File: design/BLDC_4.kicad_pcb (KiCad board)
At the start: 4 copper layers, 55 x 77 mm, 152 parts, among them J1 Conn_01x03, J2 Conn_01x02, J3 Conn_02x06_Odd_Even, J4 Conn_01x01_Pin, J5 Conn_01x01_Pin, J6 Conn_02x06_Odd_Even, K1 SERVO, P101 CANBUS, P2 SWD, P3 PWR_COMM, Q1 IRFS7530, Q2 IRFS7530, Q3 IRFS7530, Q4 IRFS7530, Q5 IRFS7530, Q6 IRFS7530, U1 STM32F40X_LQFP64, U2 TC2117, U3 DRV8302, U4 INA826AIDR, U401 SN65HVD232, U5 AM26LV32xD, U6 OPA333AIDBVR, U7 INA826AIDR, U8 MAX485ED, U9 OPA333AIDBVR, X1 MINI-USB-SHIELD-32005-201, X2 8MHz 10ppm

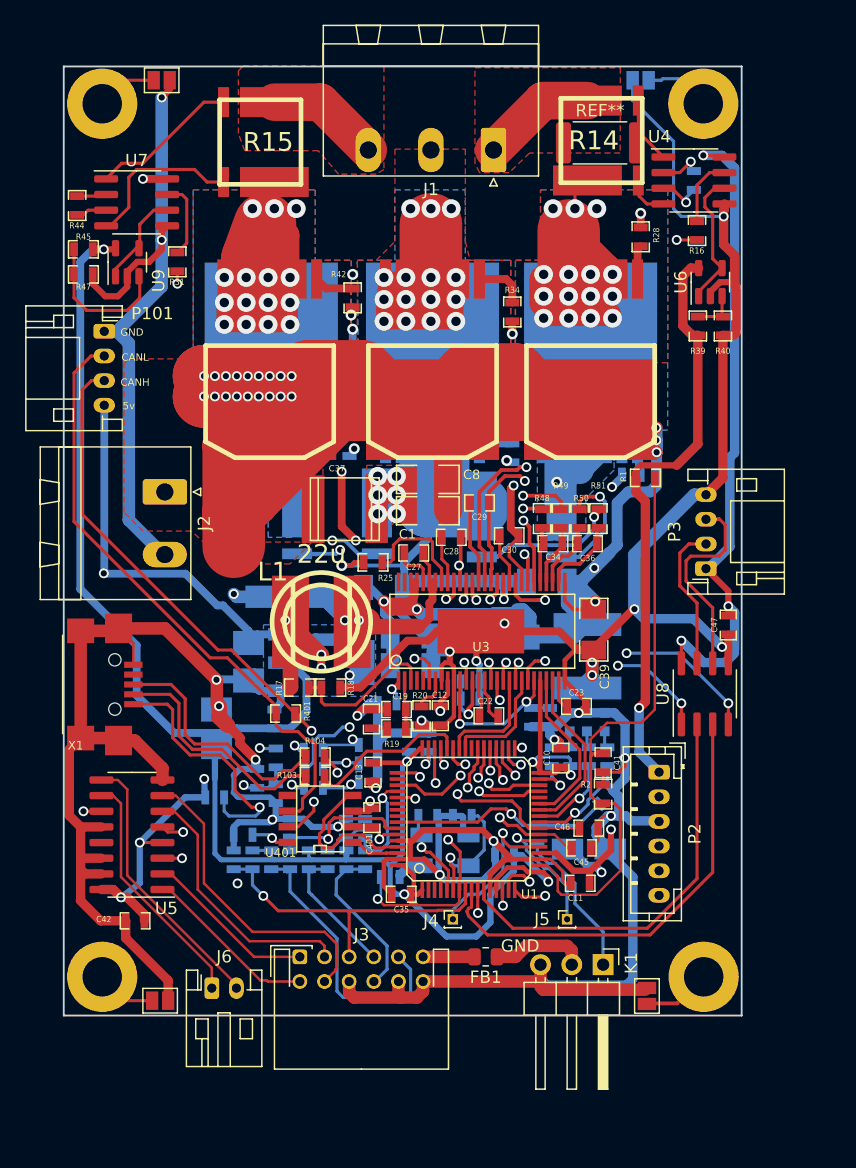
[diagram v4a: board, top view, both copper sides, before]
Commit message: Limpando warnings e DRC errors
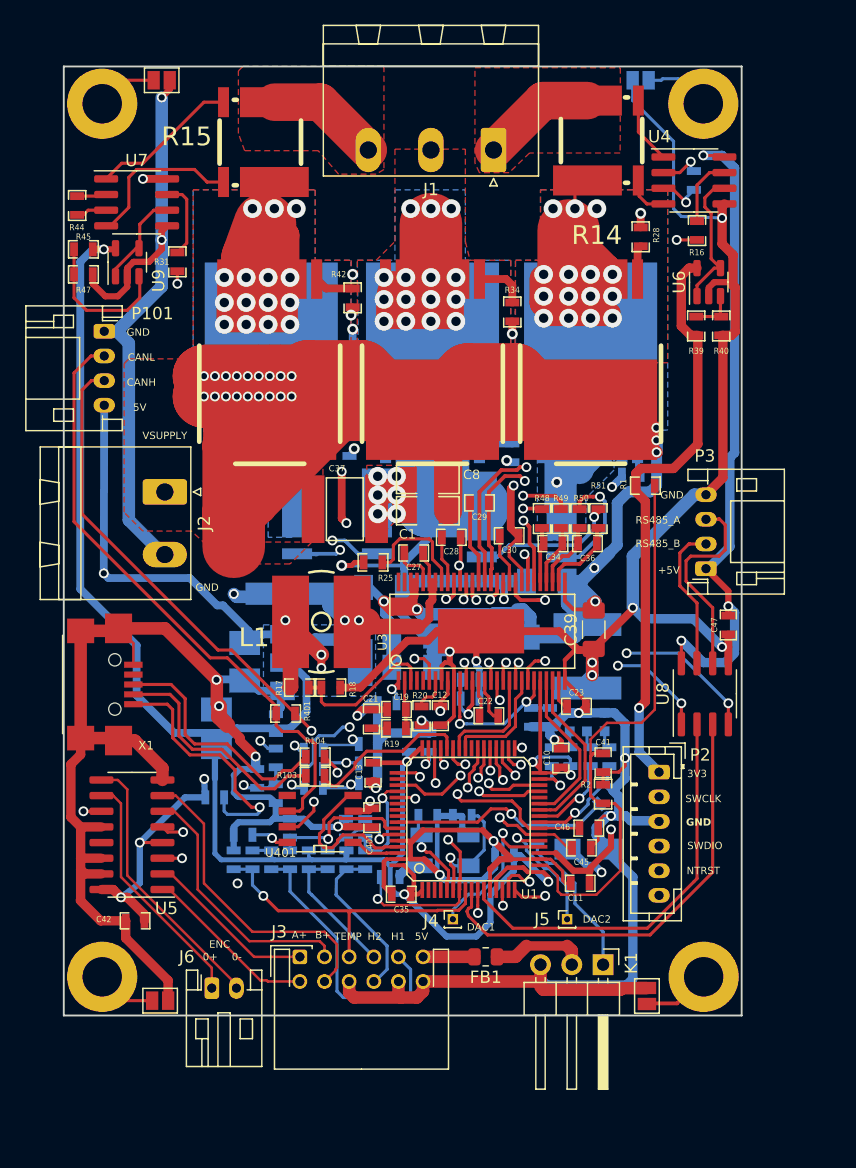
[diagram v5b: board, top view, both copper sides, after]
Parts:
- removed REF**: R_2512_6332Metric, Resistor_SMD:R_2512_6332Metric
- C25, C33: footprint w_smd_cap:c_tant_B -> CRF1:c_tant_B
- C39: footprint CRF1:SMD-1206 -> Capacitor_SMD:C_1206_3216Metric_Pad1.33x1.80mm_HandSolder
- C51: footprint w_smd_cap:c_2220 -> CRF1:c_2220
- D5: footprint w_smd_diode:do214ac -> CRF1:do214ac
- U2: footprint CRF1:SOT-223 -> Package_TO_SOT_SMD:SOT-223
- moved R1 0.64 mm to (115.2, 104.0)
- moved C24 0.40 mm to (85.2, 123.3)
- moved C33 0.32 mm to (82.7, 118.3)
- moved D4 0.25 mm to (87.0, 112.8)
- moved C49 0.18 mm to (96.3, 118.7)
- moved R37 0.17 mm to (112.3, 126.0)
- moved R38 0.14 mm to (110.7, 126.0)
- moved R39 0.13 mm to (119.3, 91.1)
- moved U6 0.13 mm to (120.3, 87.5)
- moved R40 0.13 mm to (121.3, 91.1)
- moved C26 0.13 mm to (101.0, 119.8)
- moved C44 0.13 mm to (96.3, 116.2)
- moved R24 0.09 mm to (92.7, 128.1)
- moved R33 0.08 mm to (92.7, 125.0)
- turned U2 to 0 degrees
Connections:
- C3 pad 2: GND -> /MCU/SERVO
- R39 pad 2: GND -> Net-(U6-+)
- R40 pad 1: GND -> Net-(U6-+)
- R5 pad 1: GND -> /MCU/SERVO
- U1 pad 57: GND -> /MCU/SERVO
- U6 pad 3: GND -> Net-(U6-+)
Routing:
- net GND: track 596.3 -> 566.8 mm, vias 34 -> 31
- net /MCU/SERVO: track 0.00 -> 18.1 mm, vias 0 -> 1
- net Net-(U6-+): track 0.00 -> 3.72 mm
- net VCC: track 268.6 -> 266.3 mm, vias 11 -> 10
- net /MCU/ADC_TEMP: track 48.9 -> 47.3 mm
- net V_SUPPLY: track 315.9 -> 314.8 mm
- net +5V: track 261.3 -> 260.2 mm
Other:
- board text added: "+5V"
- board text added: "0+"
- board text added: "0-"
- board text added: "3V3"
- board text added: "5V"
- board text added: "A+"
- board text added: "A-"
- board text added: "B+"
- board text added: "B-"
- board text added: "DAC1"
- board text added: "DAC2"
- board text added: "ENC"
- board text added: "NTRST"
- board text added: "RS485_A"
- board text added: "RS485_B"
- board text added: "SERVO"
- board text added: "SWCLK"
- board text added: "SWDIO"
- board text added: "VSUPPLY"
- board text removed: "3.3V"
- board text removed: "3.3v"
- board text removed: "5v"
- board text removed: "ADC"
- board text removed: "ADC2"
- board text removed: "CLK"
- board text removed: "DIO"
- board text removed: "MISO"
- board text removed: "MOSI"
- board text removed: "RST"
- board text removed: "RX"
- board text removed: "SCL"
- board text removed: "SDA"
- board text removed: "TX"

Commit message: Final 20230228
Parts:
- removed R54: SHUNT, CRF1:WSLP2726
- added JP10: SolderJumper_2_Bridged, JRM_Footprint:MicroNetSep, F.Cu at (81.9, 77.1)
- added JP11: SolderJumper_2_Bridged, JRM_Footprint:MicroNetSep, F.Cu at (112.8, 79.5)
- added JP12: SolderJumper_2_Bridged, JRM_Footprint:MicroNetSep, F.Cu at (112.8, 80.6)
- added JP5: SolderJumper_2_Bridged, JRM_Footprint:MicroNetSep, B.Cu at (104.5, 108.6)
- added JP6: SolderJumper_2_Bridged, JRM_Footprint:MicroNetSep, B.Cu at (105.4, 108.6)
- added JP7: SolderJumper_2_Bridged, JRM_Footprint:MicroNetSep, B.Cu at (89.6, 108.6)
- added JP8: SolderJumper_2_Bridged, JRM_Footprint:MicroNetSep, B.Cu at (92.3, 108.6)
- added JP9: SolderJumper_2_Bridged, JRM_Footprint:MicroNetSep, F.Cu at (81.9, 78.1)
- added R52: YLR12-3-8F-W, JRM_Footprint:YLR2512_G4, B.Cu at (104.8, 105.7)
- R14, R15, R53: value SHUNT -> YLR12-3-8F-W; footprint CRF1:WSLP2726 -> JRM_Footprint:YLR2512_G4
- U2: footprint Package_TO_SOT_SMD:SOT-223 -> CRF1:SOT-223
- moved R53 14.9 mm to (90.5, 105.7), turned to 90 degrees
- moved R14 5.62 mm to (109.3, 79.8), turned to 0 degrees
- moved R15 4.18 mm to (84.8, 79.2), turned to 0 degrees
- moved U2 0.13 mm to (88.8, 118.4), turned to 90 degrees
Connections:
- R14 pad 1: /Power MOSFETS/PHASE_1 -> /Mosfet driver/H1_VS
- R14 pad 2: /Mosfet driver/H1_VS -> /Power MOSFETS/PHASE_1
- R53 pad 1: GND -> /Mosfet driver/H3_LOW
- R53 pad 2: /Mosfet driver/H1_LOW -> GND
- U4 pad 1: Net-(U4--) -> Net-(JP11-A)
- U4 pad 4: Net-(U4-+) -> Net-(JP12-A)
- U7 pad 1: Net-(U7--) -> Net-(JP10-A)
- U7 pad 4: Net-(U7-+) -> Net-(JP9-A)
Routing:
- net Net-(JP9-A): track 0.00 -> 13.6 mm
- net Net-(U7-+): track 13.3 -> 0.00 mm
- net Net-(U7--): track 12.1 -> 0.00 mm
- net Net-(JP10-A): track 0.00 -> 10.6 mm
- net GND: track 566.8 -> 575.1 mm
- net /Mosfet driver/H1_LOW: track 48.5 -> 54.1 mm
- net Net-(U4--): track 5.41 -> 0.00 mm
- net /Power MOSFETS/PHASE_1: track 9.28 -> 14.2 mm
- net /Mosfet driver/SH1_A: track 23.9 -> 19.4 mm
- net /Mosfet driver/H3_LOW: track 57.0 -> 61.4 mm
- net /Power MOSFETS/PHASE_3: track 9.23 -> 13.3 mm
- net Net-(JP11-A): track 0.00 -> 4.06 mm
- net Net-(JP12-A): track 0.00 -> 3.96 mm
- net Net-(U4-+): track 3.53 -> 0.00 mm
- net /Mosfet driver/H3_VS: track 160.6 -> 163.6 mm
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- added copper zone on B.Cu, net GND

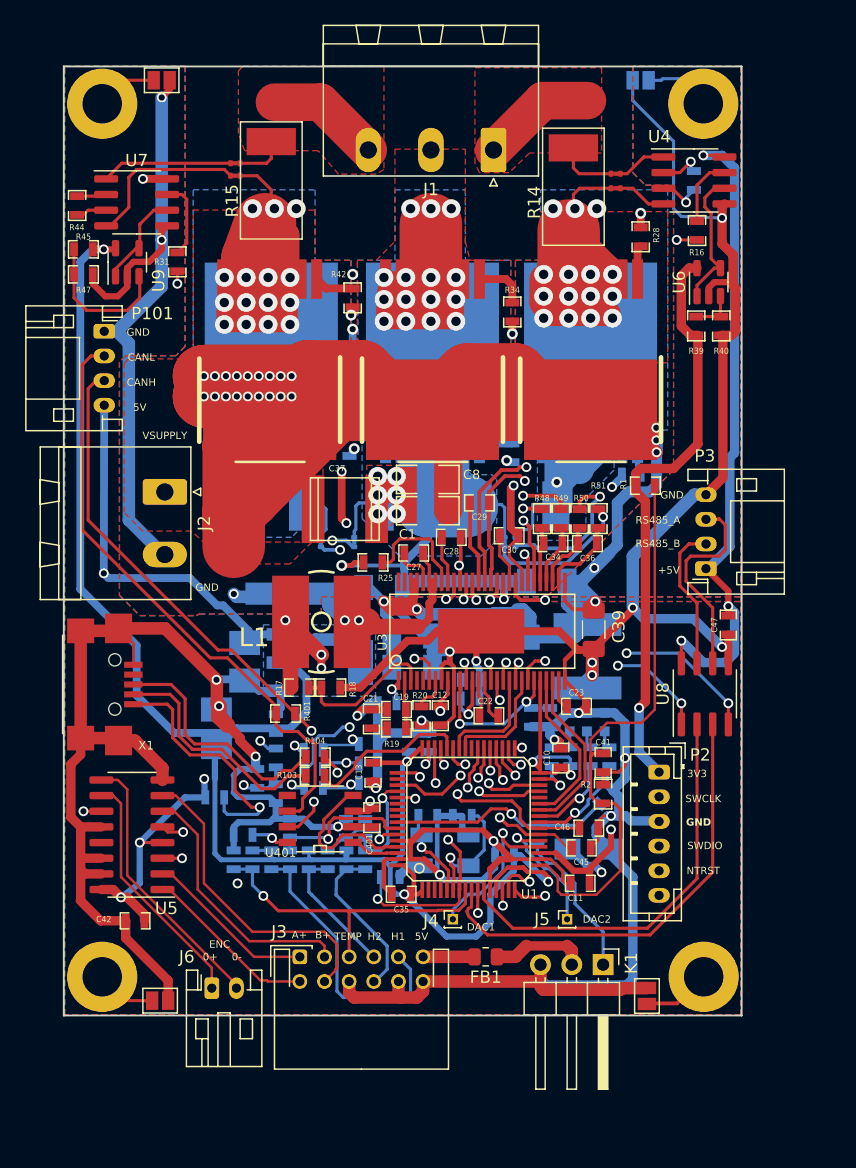
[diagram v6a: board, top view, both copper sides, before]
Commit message: Fixing voltage supply of INA826 to read phase current value
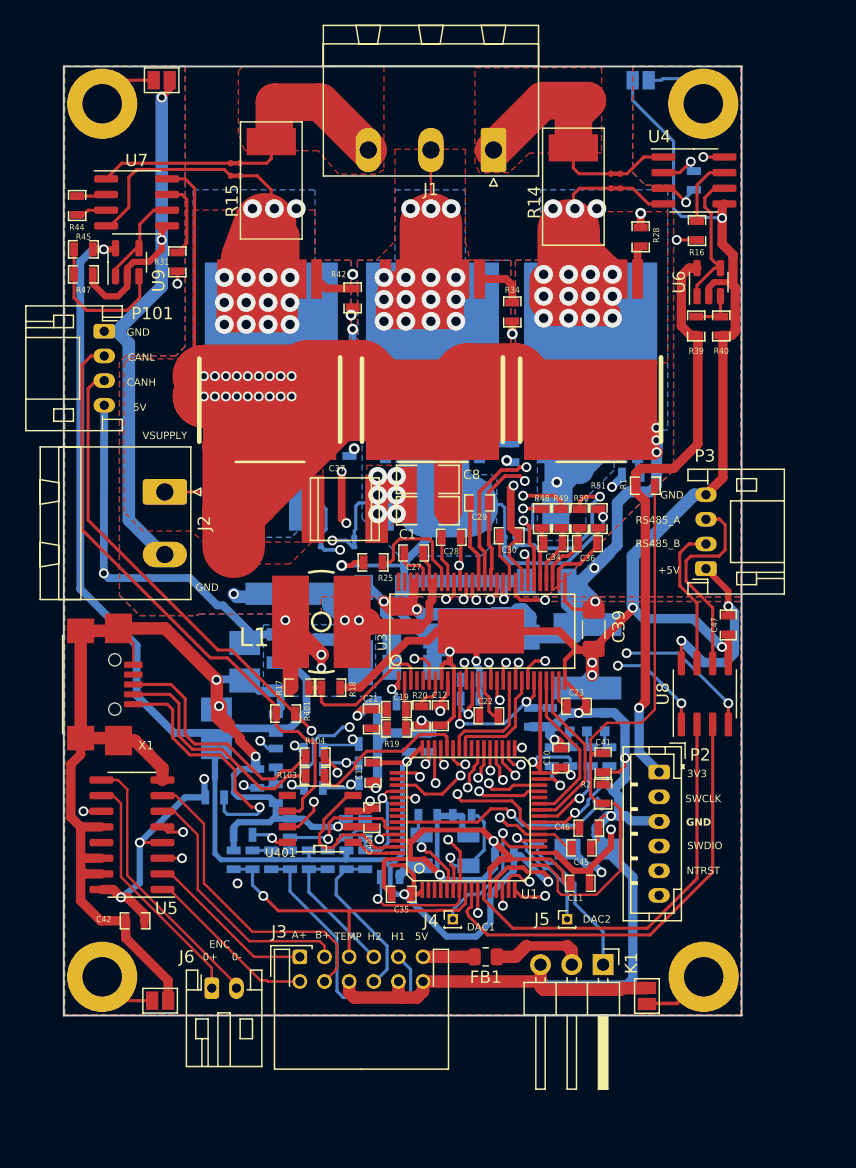
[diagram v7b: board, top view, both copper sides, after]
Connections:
- U4 pad 8: +5V -> V_SUPPLY
- U7 pad 8: +5V -> V_SUPPLY
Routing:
- net +5V: track 260.2 -> 184.2 mm, vias 13 -> 11
- net V_SUPPLY: track 314.8 -> 363.2 mm, vias 26 -> 27
- net GND: track 575.1 -> 582.0 mm
- net /Mosfet driver/H2_VS: track 145.0 -> 150.9 mm
- net /Power MOSFETS/PHASE_1: track 14.2 -> 17.7 mm
- net /Power MOSFETS/PHASE_3: track 13.3 -> 15.9 mm

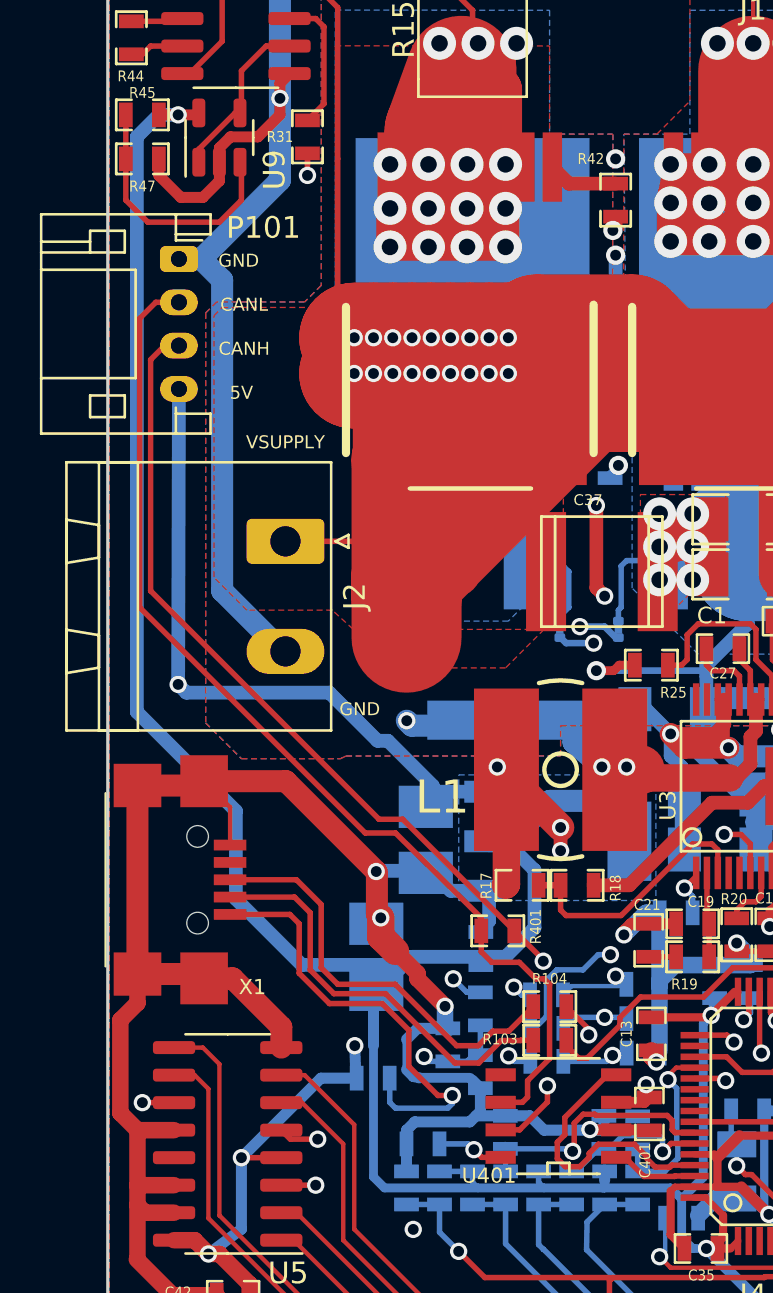
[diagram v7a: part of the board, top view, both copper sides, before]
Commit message: Fixing mini-USB connector pinout
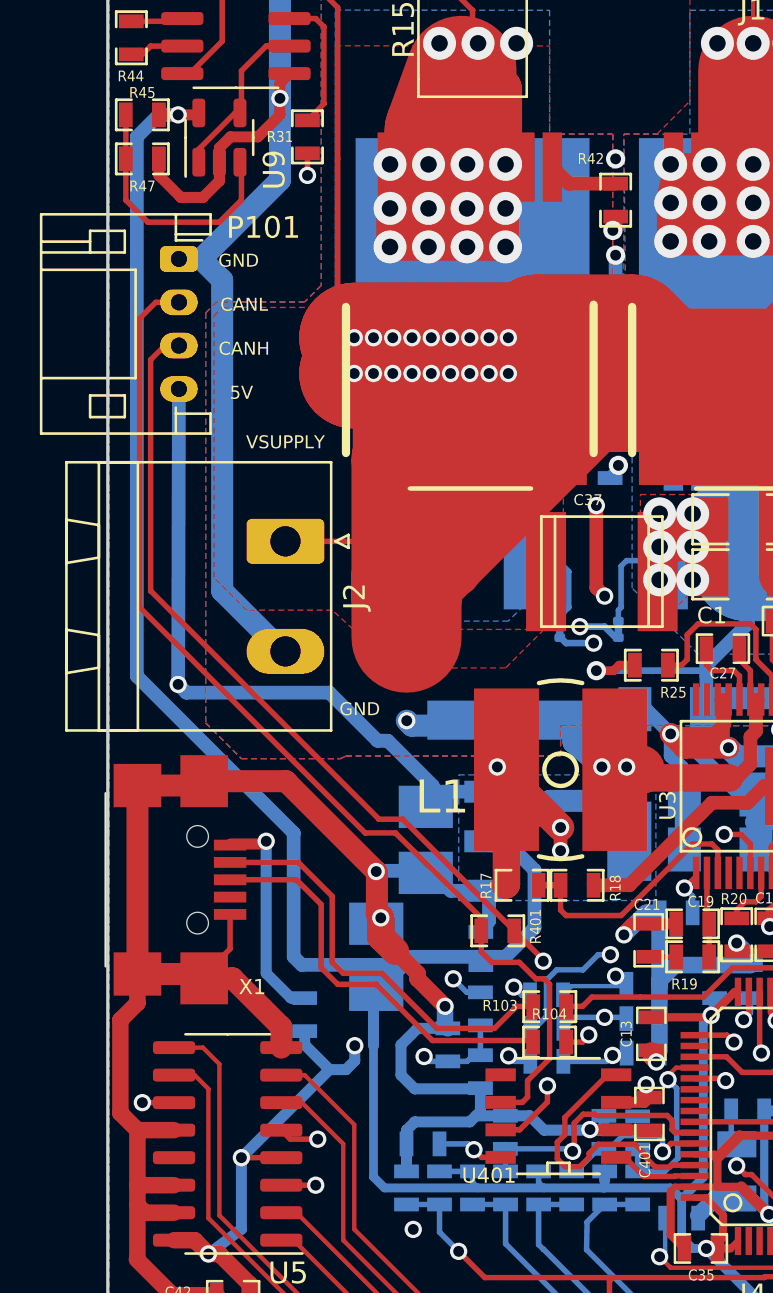
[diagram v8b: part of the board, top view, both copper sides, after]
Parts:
- moved R6 4.31 mm to (77.1, 126.4), turned to -90 degrees
- moved R104 1.64 mm to (88.4, 127.6)
- moved R103 1.55 mm to (88.4, 126.0)
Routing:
- net Net-(R6-Pad1): track 20.6 -> 10.1 mm
- net /MCU/USB_DM: track 13.3 -> 11.7 mm
- net +5V: track 184.2 -> 185.9 mm
- net Net-(R104-Pad2): track 19.6 -> 18.8 mm
